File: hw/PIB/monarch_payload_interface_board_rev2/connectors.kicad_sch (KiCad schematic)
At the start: 21 parts, among them J1 5037630291, J10 5037630491, J101 Conn_01x03, J102 Conn_01x04, J103 Conn_01x03, J104 Conn_01x02, J105 Conn_01x02, J106 Conn_01x04, J11 5037630691, J12 5037630691, J13 5037630491, J14 5037630491, J15 5037630691, J2 5037630291, J3 5037630691, J4 5037630691, J5 5037630691, J6 5037630691, J7 5037630691, J8 5037630691, J9 5037630491

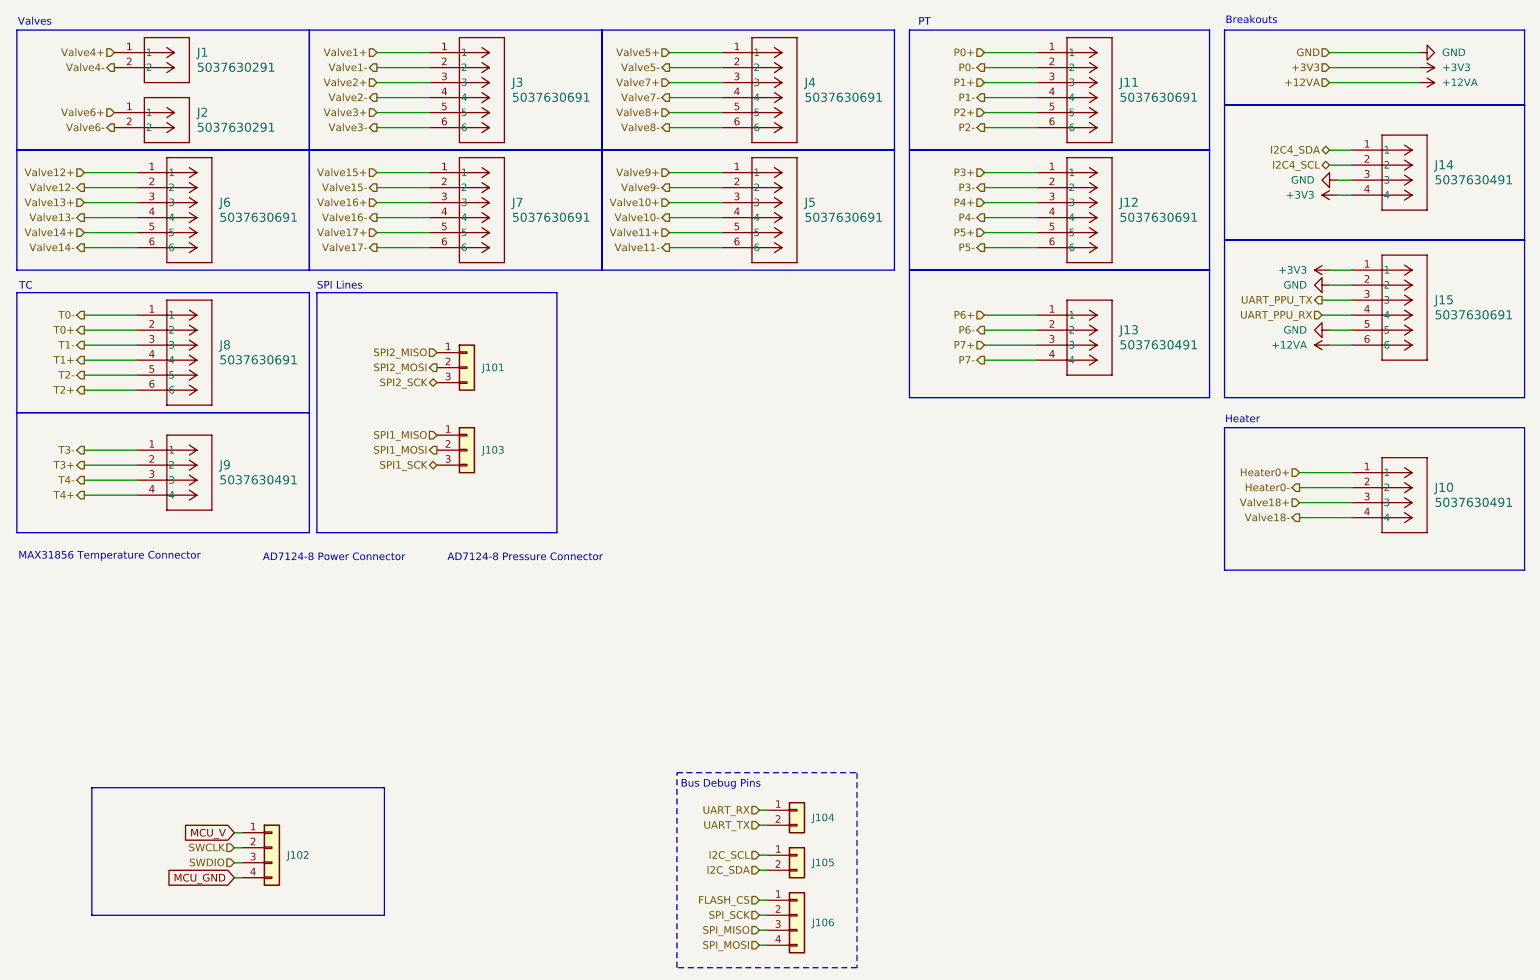
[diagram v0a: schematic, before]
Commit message: Schematic Clean Up + New Micro-Lock Plus Connectors
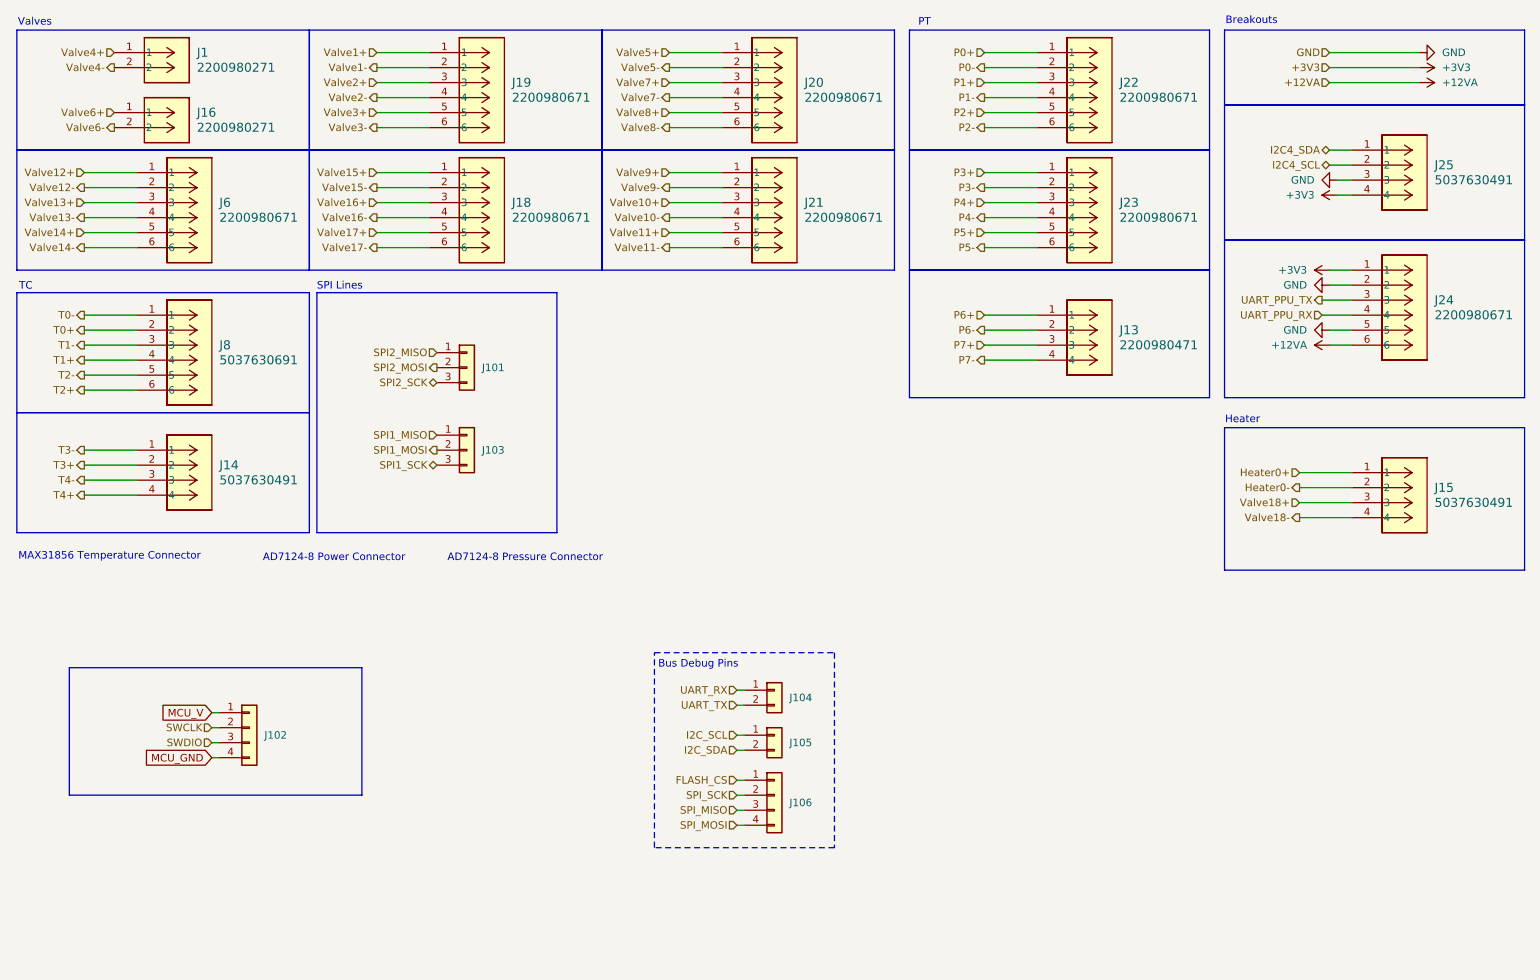
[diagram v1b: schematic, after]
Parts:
- removed J10, J9: 5037630491, 5037630491:CONN_5037630000-SD_04_MOL, symbol 5037630491:5037630491
- removed J11, J12, J15, J3, J4, J5, J7: 5037630691, 5037630691:CONN_5037630000-SD_06_MOL, symbol 5037630691:5037630691
- removed J2: 5037630291, 5037630291:CONN_5037630000-SD_02_MOL, symbol 5037630291:5037630291
- added J15, J25: 5037630491, CONN_5037630000-SD_04_MOL, symbol 5037630491:5037630491
- added J16: 2200980271, Connector_Molex_Micro-Lock-Plus:Molex_Micro-Lock_2200980271_1x02_P1.25mm_Horizontal, symbol 5037630291:5037630291
- added J18, J19, J20, J21, J22, J23, J24: 2200980671, Connector_Molex_Micro-Lock-Plus:Molex_Micro-Lock_2200980671_1x06_P1.25mm_Horizontal, symbol 5037630691:5037630691
- J1: value 5037630291 -> 2200980271; footprint 5037630291:CONN_5037630000-SD_02_MOL -> Connector_Molex_Micro-Lock-Plus:Molex_Micro-Lock_2200980271_1x02_P1.25mm_Horizontal
- J13: value 5037630491 -> 2200980471; footprint 5037630491:CONN_5037630000-SD_04_MOL -> Connector_Molex_Micro-Lock-Plus:Molex_Micro-Lock_2200980471_1x04_P1.25mm_Horizontal
- J14: footprint 5037630491:CONN_5037630000-SD_04_MOL -> CONN_5037630000-SD_04_MOL
- J6: value 5037630691 -> 2200980671; footprint 5037630691:CONN_5037630000-SD_06_MOL -> Connector_Molex_Micro-Lock-Plus:Molex_Micro-Lock_2200980671_1x06_P1.25mm_Horizontal
- J8: footprint 5037630691:CONN_5037630000-SD_06_MOL -> CONN_5037630000-SD_06_MOL
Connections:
- net +12VA: now also J24.6
- net +3V3: now also J24.1, J25.4; no longer J14.4
- net GND: now also J24.2, J24.5, J25.3; no longer J14.3
- net Heater0+: now also J15.1
- net Heater0-: now also J15.2
- net I2C4_SCL: now also J25.2; no longer J14.2
- net I2C4_SDA: now also J25.1; no longer J14.1
- net P0+: now also J22.1
- net P0-: now also J22.2
- net P1+: now also J22.3
- net P1-: now also J22.4
- net P2+: now also J22.5
- net P2-: now also J22.6
- net P3+: now also J23.1
- net P3-: now also J23.2
- net P4+: now also J23.3
- net P4-: now also J23.4
- net P5+: now also J23.5
- net P5-: now also J23.6
- net T3+: now also J14.2
- net T3-: now also J14.1
- net T4+: now also J14.4
- net T4-: now also J14.3
- net UART_PPU_RX: now also J24.4
- net UART_PPU_TX: now also J24.3
- net Valve1+: now also J19.1
- net Valve1-: now also J19.2
- net Valve10+: now also J21.3
- net Valve10-: now also J21.4
- net Valve11+: now also J21.5
- net Valve11-: now also J21.6
- net Valve15+: now also J18.1
- net Valve15-: now also J18.2
- net Valve16+: now also J18.3
- net Valve16-: now also J18.4
- net Valve17+: now also J18.5
- net Valve17-: now also J18.6
- net Valve18+: now also J15.3
- net Valve18-: now also J15.4
- net Valve2+: now also J19.3
- net Valve2-: now also J19.4
- net Valve3+: now also J19.5
- net Valve3-: now also J19.6
- net Valve5+: now also J20.1
- net Valve5-: now also J20.2
- net Valve6+: now also J16.1
- net Valve6-: now also J16.2
- net Valve7+: now also J20.3
- net Valve7-: now also J20.4
- net Valve8+: now also J20.5
- net Valve8-: now also J20.6
- net Valve9+: now also J21.1
- net Valve9-: now also J21.2
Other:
- moved on the sheet: J102, J104, J105, J106

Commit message: AD7124 Fixes
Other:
- note added: "UART Lines"
- moved on the sheet: J101, J103, J13, J15
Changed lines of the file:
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@@
 	(rectangle
 		(start 218.44 52.07)
-		(end 269.24 78.74)
+		(end 269.24 74.93)
 		(stroke
 			(width 0)
@@
 	)
 	(rectangle
-		(start 218.44 83.82)
-		(end 269.24 107.95)
+		(start 107.95 60.96)
+		(end 162.56 101.6)
+		(stroke
+			(width 0)
+			(type default)
+		)
+		(fill
+			(type none)
+		)
+	)
+	(rectangle
+		(start 165.1 78.74)
+		(end 215.9 101.6)
 		(stroke
 			(width 0)
@@
 	(rectangle
 		(start 165.1 57.15)
-		(end 215.9 78.74)
+		(end 215.9 74.93)
 		(stroke
 			(width 0)
@@
 		)
 	)
+	(text "UART Lines\n"
+		(exclude_from_sim no)
+		(at 107.696 59.436 0)
+		(effects
+			(font
+				(size 1.27 1.27)
+			)
+			(justify left top)
+		)
+	)
 	(text "AD7124-8 Power Connector"
 		(exclude_from_sim no)
-		(at 55.626 105.156 0)
+		(at 65.532 82.042 0)
 		(effects
 			(font
@@
 	(text "Heater\n"
 		(exclude_from_sim no)
-		(at 221.488 82.55 0)
+		(at 168.148 77.47 0)
 		(effects
 			(font
@@
 	(wire
 		(pts
-			(xy 231.14 96.52) (xy 240.03 96.52)
+			(xy 177.8 91.44) (xy 186.69 91.44)
 		)
 		(stroke
@@
 	(wire
 		(pts
-			(xy 177.8 64.77) (xy 186.69 64.77)
+			(xy 177.8 62.23) (xy 186.69 62.23)
 		)
 		(stroke
@@
 	(wire
 		(pts
-			(xy 231.14 99.06) (xy 240.03 99.06)
+			(xy 177.8 93.98) (xy 186.69 93.98)
 		)
 		(stroke
@@
 	(wire
 		(pts
-			(xy 231.14 93.98) (xy 240.03 93.98)
+			(xy 177.8 88.9) (xy 186.69 88.9)
 		)
 		(stroke
@@
 	(wire
 		(pts
-			(xy 177.8 67.31) (xy 186.69 67.31)
+			(xy 177.8 64.77) (xy 186.69 64.77)
 		)
 		(stroke
@@
 	(wire
 		(pts
-			(xy 177.8 72.39) (xy 186.69 72.39)
+			(xy 177.8 69.85) (xy 186.69 69.85)
 		)
 		(stroke
@@
 	(wire
 		(pts
-			(xy 177.8 69.85) (xy 186.69 69.85)
+			(xy 177.8 67.31) (xy 186.69 67.31)
 		)
 		(stroke
@@
 	(wire
 		(pts
-			(xy 231.14 91.44) (xy 240.03 91.44)
+			(xy 177.8 86.36) (xy 186.69 86.36)
 		)
 		(stroke
@@
 		)
 	)
+	(hierarchical_label "*FAULT"
+		(shape output)
+		(at 85.09 74.93 180)
+		(effects
+			(font
+				(size 1.27 1.27)
+			)
+			(justify right)
+		)
+	)
 	(hierarchical_label "UART_PPU_RX"
 		(shape input)
@@
 		)
 	)
+	(hierarchical_label "*DRDY"
+		(shape output)
+		(at 85.09 77.47 180)
+		(effects
+			(font
+				(size 1.27 1.27)
+			)
+			(justify right)
+		)
+	)
 	(hierarchical_label "SPI1_SCK"
 		(shape bidirectional)
-		(at 85.09 90.17 180)
+		(at 85.09 91.44 180)
 		(effects
 			(font
@@
 	(hierarchical_label "Valve18-"
 		(shape output)
-		(at 231.14 99.06 180)
+		(at 177.8 93.98 180)
 		(effects
 			(font
@@
 	(hierarchical_label "P7+"
 		(shape input)
-		(at 177.8 69.85 180)
+		(at 177.8 67.31 180)
 		(effects
 			(font
@@
 	(hierarchical_label "Valve18+"
 		(shape input)
-		(at 231.14 96.52 180)
+		(at 177.8 91.44 180)
 		(effects
 			(font
@@
 		)
 	)
+	(hierarchical_label "*SYNC"
+		(shape output)
+		(at 85.09 96.52 180)
+		(effects
+			(font
+				(size 1.27 1.27)
+			)
+			(justify right)
+		)
+	)
 	(hierarchical_label "Valve4+"
 		(shape input)
@@
 	(hierarchical_label "SPI2_SCK"
 		(shape bidirectional)
-		(at 85.09 76.2 180)
+		(at 85.09 72.39 180)
 		(effects
 			(font
@@
 	(hierarchical_label "P6-"
 		(shape output)
-		(at 177.8 67.31 180)
+		(at 177.8 64.77 180)
 		(effects
 			(font
@@
 	(hierarchical_label "Heater0-"
 		(shape output)
-		(at 231.14 93.98 180)
+		(at 177.8 88.9 180)
 		(effects
 			(font
@@
 	(hierarchical_label "SPI2_MOSI"
 		(shape output)
-		(at 85.09 73.66 180)
+		(at 85.09 69.85 180)
 		(effects
 			(font
@@
 		)
 	)
+	(hierarchical_label "ADC"
+		(shape output)
+		(at 85.09 93.98 180)
+		(effects
+			(font
+				(size 1.27 1.27)
+			)
+			(justify right)
+		)
+	)
 	(hierarchical_label "SPI1_MOSI"
 		(shape output)
-		(at 85.09 87.63 180)
+		(at 85.09 88.9 180)
 		(effects
 			(font
@@
 	(hierarchical_label "P7-"
 		(shape output)
-		(at 177.8 72.39 180)
+		(at 177.8 69.85 180)
 		(effects
 			(font
@@
 	(hierarchical_label "SPI2_MISO"
 		(shape input)
-		(at 85.09 71.12 180)
+		(at 85.09 67.31 180)
 		(effects
 			(font
@@
 	(hierarchical_label "SPI1_MISO"
 		(shape input)
-		(at 85.09 85.09 180)
+		(at 85.09 86.36 180)
 		(effects
 			(font
@@
 	(hierarchical_label "Heater0+"
 		(shape input)
-		(at 231.14 91.44 180)
+		(at 177.8 86.36 180)
 		(effects
 			(font
@@
 	(hierarchical_label "P6+"
 		(shape input)
-		(at 177.8 64.77 180)
+		(at 177.8 62.23 180)
 		(effects
 			(font
@@
 		(lib_name "5037630491_3")
 		(lib_id "5037630491:5037630491")
-		(at 240.03 91.44 0)
+		(at 186.69 86.36 0)
 		(unit 1)
 		(body_style 1)
@@
 		(fields_autoplaced yes)
 		(property "Reference" "J15"
-			(at 254 93.9799 0)
+			(at 200.66 88.8999 0)
 			(show_name no)
 			(do_not_autoplace no)
@@
 		)
 		(property "Value" "5037630491"
-			(at 254 96.5199 0)
+			(at 200.66 91.4399 0)
 			(show_name no)
 			(do_not_autoplace no)
@@
 		)
 		(property "Footprint" "CONN_5037630000-SD_04_MOL"
-			(at 240.03 91.44 0)
+			(at 186.69 86.36 0)
 			(hide yes)
 			(show_name no)
@@
 		)
 		(property "Datasheet" "https://www.molex.com/en-us/products/part-detail-pdf/5037630491?display=pdf"
-			(at 240.03 91.44 0)
+			(at 186.69 86.36 0)
 			(hide yes)
 			(show_name no)
@@
 		)
 		(property "Description" ""
-			(at 240.03 91.44 0)
+			(at 186.69 86.36 0)
 			(hide yes)
 			(show_name no)
@@
 		(lib_name "5037630491_2")
 		(lib_id "5037630491:5037630491")
-		(at 186.69 64.77 0)
+		(at 186.69 62.23 0)
 		(unit 1)
 		(body_style 1)
@@
 		(fields_autoplaced yes)
 		(property "Reference" "J13"
-			(at 200.66 67.3099 0)
+			(at 200.66 64.7699 0)
 			(show_name no)
 			(do_not_autoplace no)
@@
 		)
 		(property "Value" "2200980471"
-			(at 200.66 69.8499 0)
+			(at 200.66 67.3099 0)
 			(show_name no)
 			(do_not_autoplace no)
@@
 		)
 		(property "Footprint" "Connector_Molex_Micro-Lock-Plus:Molex_Micro-Lock_2200980471_1x04_P1.25mm_Horizontal"
-			(at 186.69 64.77 0)
+			(at 186.69 62.23 0)
 			(hide yes)
 			(show_name no)
@@
 		)
 		(property "Datasheet" "https://www.molex.com/en-us/products/part-detail/2200980471"
-			(at 186.69 64.77 0)
+			(at 186.69 62.23 0)
 			(hide yes)
 			(show_name no)
@@
 		)
 		(property "Description" ""
-			(at 186.69 64.77 0)
+			(at 186.69 62.23 0)
 			(hide yes)
 			(show_name no)
@@
 	(symbol
 		(lib_id "Connector_Generic:Conn_01x03")
-		(at 90.17 73.66 0)
+		(at 90.17 69.85 0)
 		(unit 1)
 		(body_style 1)
@@
 		(dnp no)
 		(property "Reference" "J101"
-			(at 92.71 73.66 0)
+			(at 92.71 69.85 0)
 			(show_name no)
 			(do_not_autoplace no)
@@
 		)
 		(property "Value" "Conn_01x03"
-			(at 81.534 79.502 0)
+			(at 81.534 75.692 0)
 			(hide yes)
 			(show_name no)
@@
 		)
 		(property "Footprint" "Connector_PinHeader_1.27mm:PinHeader_1x03_P1.27mm_Vertical"
-			(at 90.17 73.66 0)
+			(at 90.17 69.85 0)
 			(hide yes)
 			(show_name no)
@@
 		)
 		(property "Datasheet" ""
-			(at 90.17 73.66 0)
+			(at 90.17 69.85 0)
 			(hide yes)
 			(show_name no)
@@
 		)
 		(property "Description" "Generic connector, single row, 01x03, script generated (kicad-library-utils/schlib/autogen/connector/)"
-			(at 90.17 73.66 0)
+			(at 90.17 69.85 0)
 			(hide yes)
 			(show_name no)
@@
 	(symbol
 		(lib_id "Connector_Generic:Conn_01x03")
-		(at 90.17 87.63 0)
+		(at 90.17 88.9 0)
 		(unit 1)
 		(body_style 1)
@@
 		(dnp no)
 		(property "Reference" "J103"
-			(at 92.71 87.63 0)
+			(at 92.71 88.9 0)
 			(show_name no)
 			(do_not_autoplace no)
@@
 		)
 		(property "Value" "Conn_01x03"
-			(at 81.534 93.472 0)
+			(at 81.534 94.742 0)
 			(hide yes)
 			(show_name no)
@@
 		)
 		(property "Footprint" "Connector_PinHeader_1.27mm:PinHeader_1x03_P1.27mm_Vertical"
-			(at 90.17 87.63 0)
+			(at 90.17 88.9 0)
 			(hide yes)
 			(show_name no)
@@
 		)
 		(property "Datasheet" ""
-			(at 90.17 87.63 0)
+			(at 90.17 88.9 0)
 			(hide yes)
 			(show_name no)
@@
 		)
 		(property "Description" "Generic connector, single row, 01x03, script generated (kicad-library-utils/schlib/autogen/connector/)"
-			(at 90.17 87.63 0)
+			(at 90.17 88.9 0)
 			(hide yes)
 			(show_name no)

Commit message: Connector Footprints / Additions + Validated MAX31856
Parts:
- removed J101, J103: Conn_01x03, Connector_PinHeader_1.27mm:PinHeader_1x03_P1.27mm_Vertical, symbol Connector_Generic:Conn_01x03
- removed J102: Conn_01x04, Connector_PinHeader_2.54mm:PinHeader_1x04_P2.54mm_Vertical, symbol Connector_Generic:Conn_01x04
- removed J104: Conn_01x02, Connector_PinHeader_2.54mm:PinHeader_1x02_P2.54mm_Vertical, symbol Connector_Generic:Conn_01x02
- removed J105: Conn_01x02, Connector_PinHeader_1.27mm:PinHeader_1x02_P1.27mm_Vertical, symbol Connector_Generic:Conn_01x02
- removed J106: Conn_01x04, Connector_PinHeader_1.27mm:PinHeader_1x04_P1.27mm_Vertical, symbol Connector_Generic:Conn_01x04
- added J2: Conn_01x06, Connector_PinHeader_1.27mm:PinHeader_1x06_P1.27mm_Vertical, symbol Connector_Generic:Conn_01x06
- added J3: Conn_01x05, Connector_PinHeader_1.00mm:PinHeader_1x05_P1.00mm_Vertical, symbol Connector_Generic:Conn_01x05
- added J4: Conn_01x04, Connector_PinHeader_1.00mm:PinHeader_1x04_P1.00mm_Vertical, symbol Connector_Generic:Conn_01x04
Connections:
- net *DRDY: now also J2.5 (Pin_5)
- net *FAULT: now also J2.4 (Pin_4)
- net *SYNC: now also J3.5 (Pin_5)
- net ADC: now also J3.4 (Pin_4)
- net SPI1_MISO: now also J3.1 (Pin_1)
- net SPI1_MOSI: now also J3.2 (Pin_2)
- net SPI1_SCK: now also J3.3 (Pin_3)
- net SPI2_MISO: now also J2.1 (Pin_1)
- net SPI2_MOSI: now also J2.2 (Pin_2)
- net SPI2_SCK: now also J2.3 (Pin_3)
- new net T1: J2.6 (Pin_6)
- new net UART4_RX: J4.1 (Pin_1)
- new net UART4_TX: J4.2 (Pin_2)
- new net USART3_RX: J4.3 (Pin_3)
- new net USART3_TX: J4.4 (Pin_4)
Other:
- note removed: "Bus Debug Pins"
